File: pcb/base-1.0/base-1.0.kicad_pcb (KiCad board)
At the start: 2 copper layers, 85.6 x 54 mm, 178 parts, among them J101 USB_B_Micro, J102 UART, J103 74984104400, J104 Jack-DC, J105 USB_GPIO, J106 RPI_HEADER, Q101 BC817, Q102 BC817, Q103 DMP2305U-7, Q201 IRF7324TRPBF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

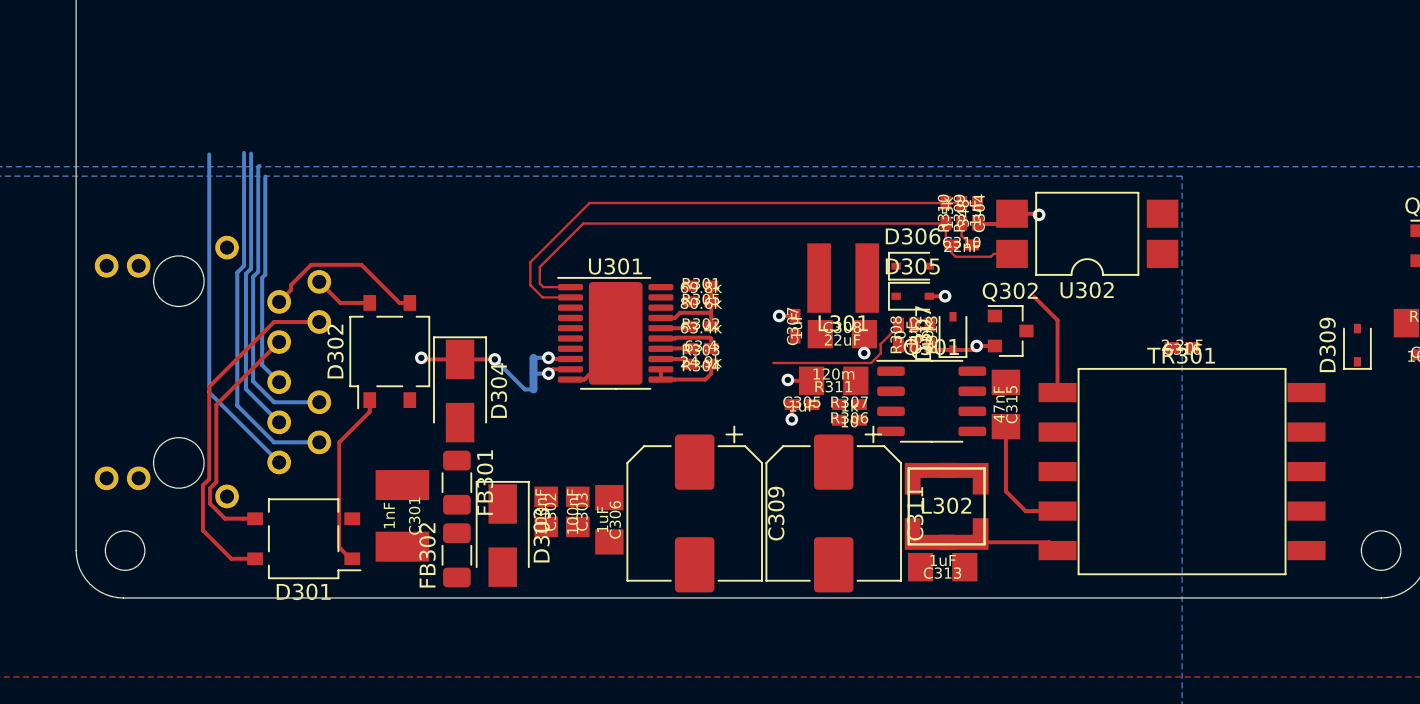
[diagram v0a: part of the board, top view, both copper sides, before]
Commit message: o Placing most of POE parts.
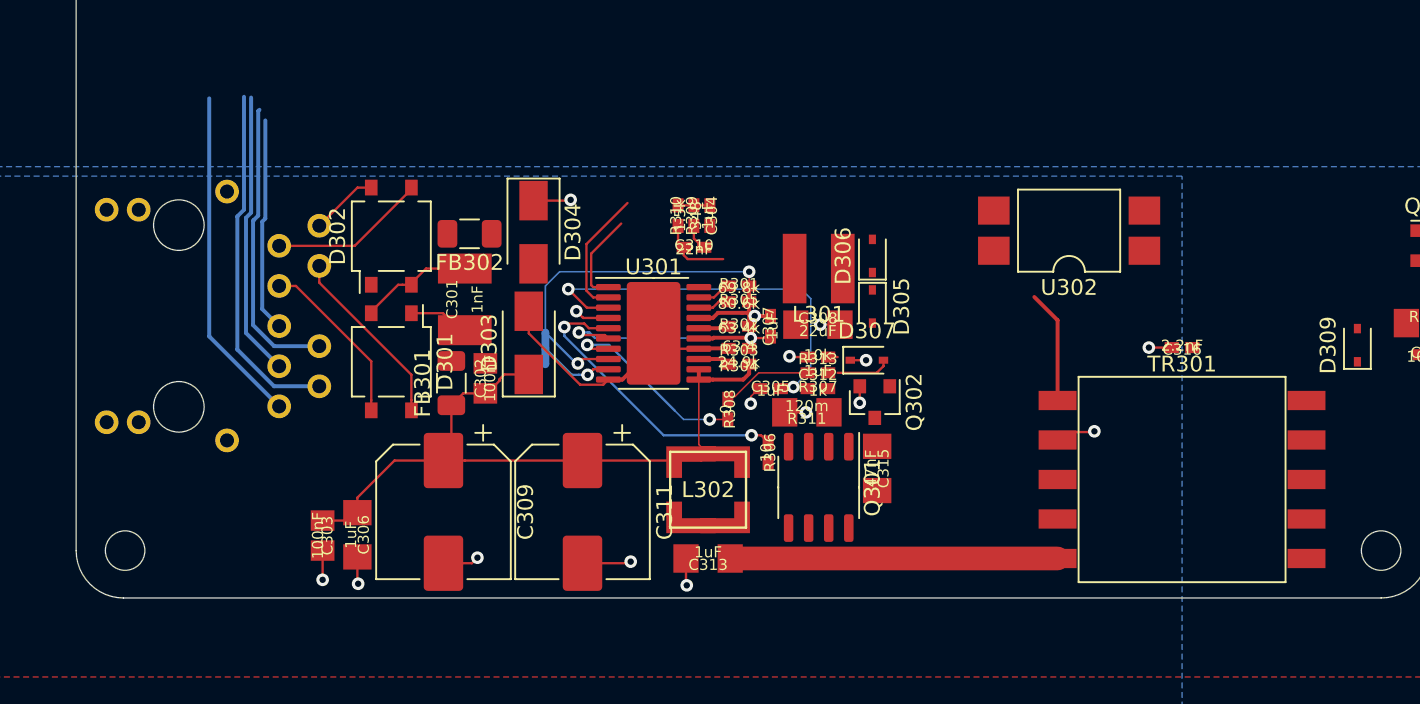
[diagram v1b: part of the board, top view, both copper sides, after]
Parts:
- moved FB302 20.4 mm to (132.9, 108.0), turned to 180 degrees
- moved R309 17.0 mm to (147.1, 106.8)
- moved R310 17.0 mm to (146.1, 106.8)
- moved C304 17.0 mm to (148.1, 106.8)
- moved C310 17.0 mm to (147.1, 108.8)
- moved C303 16.2 mm to (123.6, 127.0)
- moved C306 16.0 mm to (125.8, 127.0)
- moved C309 15.9 mm to (131.2, 125.5)
- moved C311 15.9 mm to (140.1, 125.5)
- moved L302 15.1 mm to (148.0, 124.2)
- moved C313 14.9 mm to (148.0, 128.5)
- moved C301 14.3 mm to (132.6, 112.1), turned to 90 degrees
- moved D301 12.5 mm to (128.0, 116.0), turned to 270 degrees
- moved D303 12.3 mm to (136.7, 114.8), turned to 90 degrees
- moved R308 11.8 mm to (149.2, 119.0), turned to 270 degrees
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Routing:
- net /PoE/ETH_VDD: track 4.59 -> 45.7 mm
- net /PoE/CS: track 0.00 -> 26.5 mm, vias 0 -> 2
- net /PoE/CTL: track 35.9 -> 10.4 mm
- net /PoE/VB: track 34.2 -> 10.2 mm
- net /PoE/ARTN: track 8.07 -> 27.7 mm, vias 1 -> 2
- net /PoE/GATE: track 0.00 -> 19.3 mm, vias 0 -> 2
- net /PoE/VC: track 0.00 -> 14.3 mm, vias 0 -> 2
- net Net-(C313-Pad1): track 7.24 -> 20.7 mm
- net /PoE/ETH_VSS: track 6.53 -> 17.7 mm
- net /PoE/Vin_A2: track 22.0 -> 11.6 mm
- net Net-(C315-Pad2): track 7.89 -> 0.00 mm
- net Net-(C301-Pad1): track 11.2 -> 3.95 mm
- net Net-(C301-Pad2): track 0.00 -> 7.21 mm
- net Net-(C312-Pad2): track 0.00 -> 5.32 mm
- net GND_ETH: track 22.1 -> 27.1 mm, vias 9 -> 16
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
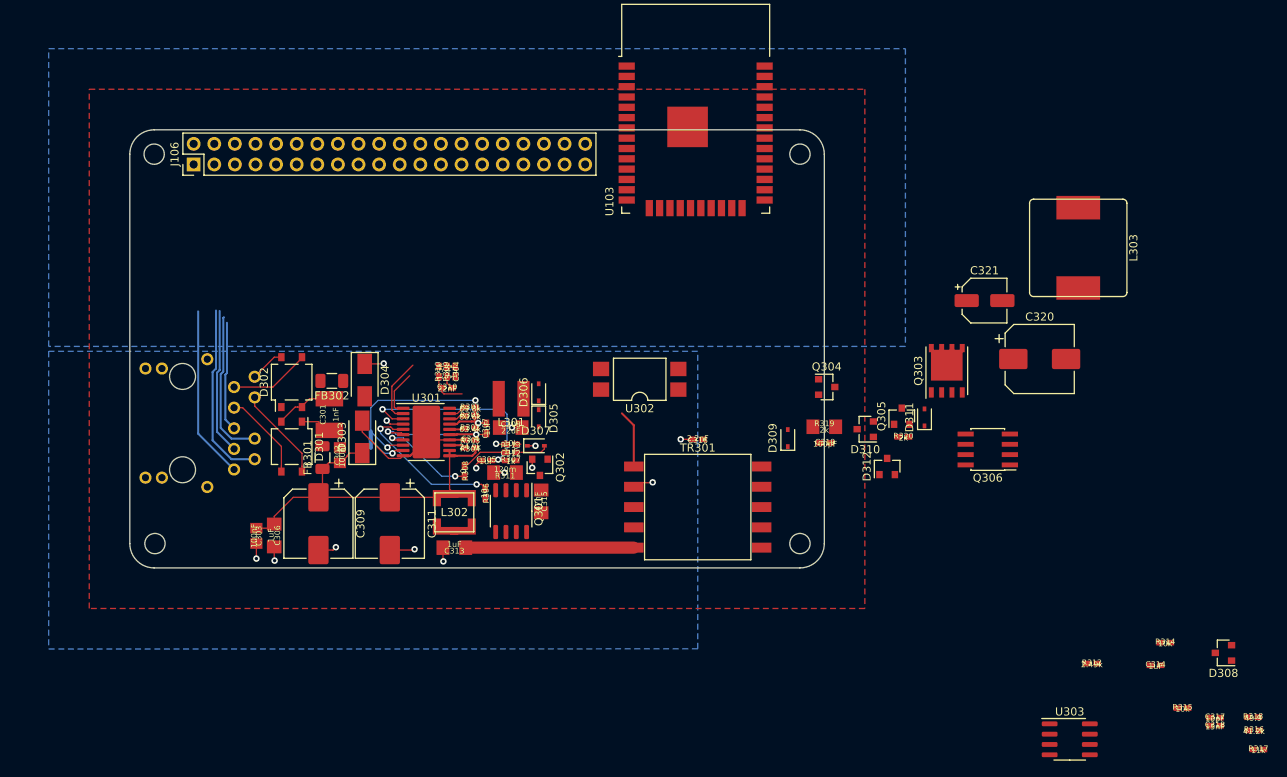
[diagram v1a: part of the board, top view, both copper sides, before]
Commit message: o Adjusting a couple of symbols. o PoE done for now.
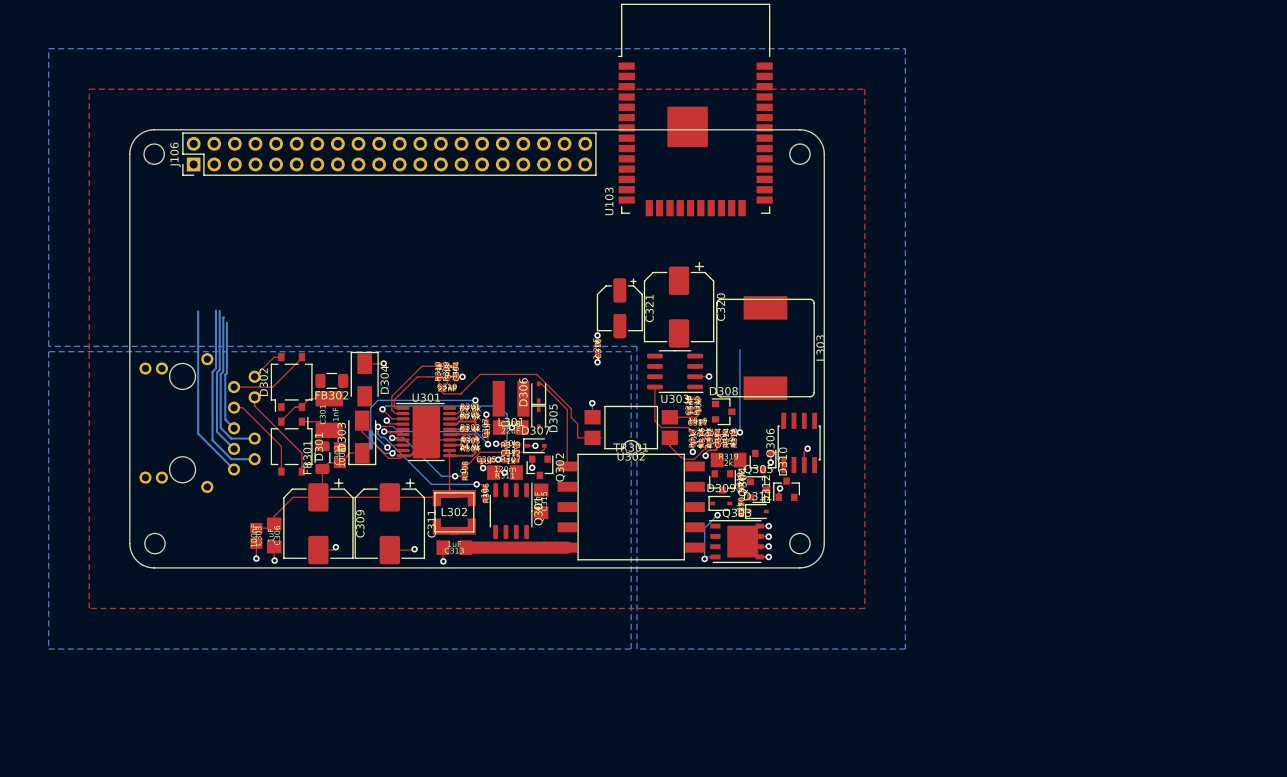
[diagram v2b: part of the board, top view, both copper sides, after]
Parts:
- moved R317 79.6 mm to (177.4, 115.0), turned to 90 degrees
- moved R316 77.1 mm to (178.4, 115.0), turned to 270 degrees
- moved C318 75.8 mm to (177.0, 111.0), turned to 90 degrees
- moved C317 73.4 mm to (178.0, 113.0), turned to 180 degrees
- moved R318 72.7 mm to (182.4, 115.0), turned to 270 degrees
- moved R315 70.4 mm to (178.0, 111.0), turned to 90 degrees
- moved D308 68.4 mm to (181.2, 111.8), turned to 0 degrees
- moved U303 66.5 mm to (175.2, 106.8), turned to 180 degrees
- moved C314 60.9 mm to (180.4, 115.0), turned to 270 degrees
- moved R314 59.8 mm to (181.4, 115.0), turned to 270 degrees
- moved R312 54.8 mm to (179.4, 115.0), turned to 270 degrees
- moved C321 45.0 mm to (168.4, 99.0), turned to 270 degrees
- moved C320 44.9 mm to (175.7, 98.8), turned to 270 degrees
- moved L303 40.5 mm to (186.3, 103.9)
- moved Q303 33.3 mm to (182.8, 127.8), turned to 0 degrees
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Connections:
- Q303 pad 1: GND -> /PoE/T_NEG
- Q303 pad 2: Net-(D309-Pad2) -> /PoE/T_NEG
- Q303 pad 4: (no net) -> Net-(D309-Pad2)
- Q303 pad 5: (no net) -> GND
- Q306 pad 1: /PoE/T_POS -> GND
- Q306 pad 2: Net-(D311-Pad2) -> GND
- Q306 pad 4: (no net) -> Net-(D311-Pad2)
- Q306 pad 5: (no net) -> /PoE/T_POS
- Q306 pad 6: (no net) -> /PoE/T_POS
- Q306 pad 7: (no net) -> /PoE/T_POS
- Q306 pad 8: (no net) -> /PoE/T_POS
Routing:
- net /PoE/CTL: track 10.4 -> 35.5 mm
- net GND: track 0.00 -> 17.7 mm, vias 0 -> 11
- net /Power mux/Vin_PoE: track 0.00 -> 11.0 mm, vias 0 -> 1
- net Net-(C317-Pad1): track 0.00 -> 9.52 mm
- net Net-(C313-Pad1): track 20.7 -> 12.5 mm
- net Net-(R312-Pad2): track 0.00 -> 7.51 mm
- net Net-(D309-Pad2): track 0.00 -> 7.49 mm, vias 0 -> 2
- net Net-(D306-Pad2): track 6.66 -> 11.8 mm
- net Net-(D308-Pad2): track 0.00 -> 4.78 mm
- net Net-(C317-Pad2): track 0.00 -> 4.71 mm
- net /PoE/VC: track 14.3 -> 17.3 mm
- net /PoE/VB: track 10.2 -> 12.6 mm
- net /PoE/GATE: track 19.3 -> 20.1 mm
- net GND_ETH: track 27.1 -> 26.8 mm, vias 16 -> 17
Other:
- net class Power added: clearance 0.2, trace_width 0.2, via_dia 0.8, via_drill 0.4

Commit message: o Much more PCB work.
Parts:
- RN101: value R_Network04 -> 49.9 Ω; footprint Resistor_THT:R_Array_SIP5 -> Resistor_SMD:R_Array_Convex_4x1206
- moved C102 204.1 mm to (227.8, 75.2)
- moved C101 163.8 mm to (226.3, 71.0)
- moved RN101 139.1 mm to (143.4, 103.7), turned to 180 degrees
- moved C114 136.3 mm to (162.7, 86.0)
- moved Q103 113.3 mm to (156.7, 104.0)
- moved U102 111.6 mm to (148.3, 103.9), turned to 90 degrees
- moved SW101 110.8 mm to (162.4, 89.9)
- moved C104 108.0 mm to (118.4, 125.3), turned to 180 degrees
- moved J102 103.3 mm to (126.7, 102.4), turned to 90 degrees
- moved U107 103.1 mm to (155.4, 86.7)
- moved Q203 102.2 mm to (161.5, 99.2)
- moved J101 101.9 mm to (109.5, 99.6), turned to 270 degrees
- moved R119 101.6 mm to (152.4, 102.9), turned to 180 degrees
- moved R118 99.9 mm to (152.4, 105.9), turned to 180 degrees
- moved R117 98.3 mm to (152.4, 104.9), turned to 180 degrees
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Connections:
- net Net-(NT201-Pad1) renamed /Power mux/Vin_PoE_sel
- net Net-(NT201-Pad2) renamed /Power mux/Vin_adapter_sel
- net Net-(NT201-Pad3) renamed /Power mux/Vin_USB_sel
- net Net-(U101-Pad3) renamed /D+
- net Net-(U101-Pad4) renamed /D-
- C107 pad 1: +3V3 -> +3V3_PHY
- C108 pad 1: +3V3 -> +3V3_PHY
- C120 pad 1: /BOOT -> /BOOT_3.3V
- C120 pad 2: /SW -> /SW_3.3V
- C121 pad 1: /BOOT -> /BOOT_12V
- C121 pad 2: /SW -> /SW_12V
- C122 pad 2: /FB -> /FB_3.3V
- C123 pad 2: /FB -> /FB_12V
- FB101 pad 2: +3V3 -> +3V3_PHY
- L101 pad 2: /SW -> /SW_3.3V
- L102 pad 2: /SW -> /SW_12V
- Q103 pad 1: +3V3 -> +3V3_PHY
- R103 pad 2: /FB -> /FB_3.3V
- R105 pad 1: /FB -> /FB_3.3V
- R109 pad 1: +3V3 -> +3V3_PHY
- R111 pad 2: /FB -> /FB_12V
- R116 pad 2: +3V3 -> +3V3_PHY
- R117 pad 1: +3V3 -> +3V3_PHY
- R118 pad 1: +3V3 -> +3V3_PHY
- R119 pad 1: +3V3 -> +3V3_PHY
- R120 pad 1: +3V3 -> +3V3_PHY
- R121 pad 1: /FB -> /FB_12V
- RN101 pad 1: +3V3 -> /ETH_RD+
- RN101 pad 3: /ETH_RD+ -> /ETH_TD+
- RN101 pad 5: /ETH_TD+ -> +3V3_PHY
- U102 pad 9: +3V3 -> +3V3_PHY
- U104 pad 1: Net-(J101-Pad2) -> Net-(J101-Pad3)
- U104 pad 6: Net-(J101-Pad3) -> Net-(J101-Pad2)
- U105 pad 2: /SW -> /SW_3.3V
- U105 pad 4: /FB -> /FB_3.3V
- U105 pad 6: /BOOT -> /BOOT_3.3V
- U106 pad 2: /SW -> /SW_12V
- U106 pad 4: /FB -> /FB_12V
- U106 pad 6: /BOOT -> /BOOT_12V
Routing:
- net /USB_TX: track 0.00 -> 21.7 mm, vias 0 -> 1
- net /Power mux/Vin_USB: track 0.00 -> 20.0 mm, vias 0 -> 2
- net +3V3: track 0.00 -> 19.6 mm, vias 0 -> 2
- net /USB_RX: track 0.00 -> 18.7 mm, vias 0 -> 1
- net Net-(C104-Pad1): track 18.0 -> 0.00 mm
- net /MCU_IO0: track 0.00 -> 13.1 mm
- net GND: track 17.7 -> 29.4 mm, vias 11 -> 17
- net /PoE/CTL: track 35.5 -> 24.8 mm
- net /RTS: track 0.00 -> 10.1 mm
- net /DTR: track 0.00 -> 9.93 mm
- net /MCU_RESET: track 0.00 -> 8.88 mm
- net /PoE/Vin_A1: track 10.9 -> 19.7 mm
- net /Power mux/Vin_adapter: track 0.00 -> 8.58 mm
- net Net-(R101-Pad2): track 0.00 -> 8.37 mm
- net /ETH_TD+: track 21.3 -> 13.8 mm
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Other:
- net class Default: via_dia 0.8 -> 0.5; via_drill 0.4 -> 0.25
- net class Power: via_drill 0.4 -> 0.3
- net class Power_0.8 added: clearance 0.3, trace_width 0.8, via_dia 0.8, via_drill 0.3
- rule via_min_drill: 0.3 -> 0.249
- rule via_min_size: 0.4 -> 0.25

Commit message: o More PCB work.
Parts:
- removed C109: 1uF, IPC-7351-CAPC:CAPC_1005x015
- removed NT301: Net-Tie_3_Tee, NetTie:NetTie-3_SMD_Pad0.5mm
- removed RN101: 49.9 Ω, Resistor_SMD:R_Array_Convex_4x1206
- added NT202: Net-Tie_2, NetTie:NetTie-2_SMD_Pad0.5mm, B.Cu at (152.2, 110.6)
- added NT203: Net-Tie_2, NetTie:NetTie-2_SMD_Pad0.5mm, F.Cu at (139.7, 116.5)
- added R124: 49.9, IPC-7351-RESC:RESC_1005x015, F.Cu at (143.8, 101.8)
- added R125: 49.9, IPC-7351-RESC:RESC_1005x015, F.Cu at (144.8, 101.8)
- added R126: 49.9, IPC-7351-RESC:RESC_1005x015, F.Cu at (141.8, 101.8)
- added R127: 49.9, IPC-7351-RESC:RESC_1005x015, F.Cu at (142.8, 101.8)
- TP101: moved to B.Cu
- moved C105 144.4 mm to (150.3, 108.4), turned to 270 degrees
- moved C111 133.8 mm to (146.2, 99.8), turned to 90 degrees
- moved FB101 112.6 mm to (145.9, 108.2), turned to 270 degrees
- moved C108 107.1 mm to (158.8, 103.8), turned to 90 degrees
- moved C112 104.6 mm to (148.3, 108.4), turned to 270 degrees
- moved C106 104.0 mm to (149.3, 108.4), turned to 270 degrees
- moved C107 103.1 mm to (152.4, 104.3)
- moved C110 102.3 mm to (147.3, 108.4), turned to 270 degrees
- moved TP101 98.7 mm to (151.8, 107.3)
- moved R108 97.1 mm to (144.4, 108.0), turned to 270 degrees
- moved R116 89.4 mm to (112.6, 122.1)
- moved R115 76.3 mm to (112.8, 104.7), turned to 180 degrees
- moved C113 72.1 mm to (109.8, 104.7)
- moved C114 34.0 mm to (174.6, 54.2)
- moved SW101 34.0 mm to (174.3, 58.1)
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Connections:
- net Net-(J101-Pad3) renamed /IN_D+
- C108 pad 1: +3V3_PHY -> +3V3
- D302 pad 4: /PoE/Vin_B2 -> /PoE/Vin_A1
- J101 pad 2: Net-(J101-Pad2) -> /IN_D-
- J103 pad 10: /PoE/Vin_B2 -> /PoE/Vin_A1
- J106 pad 11: /EXP_B1 -> /EXP_B6
- J106 pad 13: /EXP_B7 -> /EXP_B5
- J106 pad 15: /EXP_B2 -> /EXP_B4
- J106 pad 18: /EXP_B4 -> /EXP_B2
- J106 pad 21: /EXP_A7 -> /EXP_B1
- J106 pad 22: /EXP_B5 -> /EXP_B0
- J106 pad 24: /EXP_A6 -> /EXP_A7
- J106 pad 26: /EXP_A5 -> /EXP_A6
- J106 pad 27: /EXP_A0 -> /EXP_A5
- J106 pad 28: /EXP_A1 -> /EXP_A4
- J106 pad 31: /EXP_A4 -> /EXP_A2
- J106 pad 36: /EXP_B0 -> /EXP_A1
- J106 pad 37: /EXP_B6 -> /EXP_A0
- J106 pad 7: /EXP_A2 -> /EXP_B7
- R116 pad 2: +3V3_PHY -> /PHY_VDDA
- U102 pad 2: /ETH_GREEN_N -> /ETH_YELLOW_P
- U102 pad 3: /ETH_YELLOW_P -> /ETH_GREEN_N
- U104 pad 3: /D- -> /IN_D-
- U104 pad 4: /D+ -> /D-
- U104 pad 5: /Power mux/Vin_USB -> Net-(FB102-Pad2)
- U104 pad 6: Net-(J101-Pad2) -> /D+
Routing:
- net /ETH_YELLOW_P: track 0.00 -> 63.9 mm, vias 0 -> 1
- net /ETH_GREEN_N: track 0.00 -> 46.7 mm, vias 0 -> 1
- net GND: track 29.4 -> 47.7 mm, vias 17 -> 25
- net /EXP_B7: track 0.00 -> 14.9 mm
- net /MCU_IO0: track 13.1 -> 0.00 mm
- net /ETH_TD-: track 15.2 -> 2.36 mm, vias 0 -> 1
- net /PHY_VDDA: track 0.00 -> 12.4 mm, vias 0 -> 2
- net /IN_D-: track 0.00 -> 12.0 mm
- net /EXP_A6: track 0.00 -> 10.7 mm
- net /EXP_A5: track 0.00 -> 10.4 mm
- net /ETH_TD+: track 13.8 -> 3.88 mm, vias 0 -> 1
- net /IN_D+: track 2.46 -> 12.1 mm
- net /ETH_RD-: track 7.33 -> 16.8 mm, vias 0 -> 1
- net /PoE/CTL: track 24.8 -> 34.3 mm, vias 0 -> 2
- net /EXP_B0: track 0.00 -> 9.47 mm
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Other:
- net class Power_0.6 added: clearance 0.3, trace_width 0.6, via_dia 0.5, via_drill 0.25
- net class Power_0.8: clearance 0.3 -> 0.2
- net class Size_0.2__0.5 added: clearance 0.2, trace_width 0.2, via_dia 0.5, via_drill 0.25

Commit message: o More PCB work.
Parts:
- NT101, NT102, NT203: footprint NetTie:NetTie-2_SMD_Pad0.5mm -> UnlockOslo:NetTie-2_SMD_Pad0.15mm
- NT202: footprint NetTie:NetTie-2_SMD_Pad0.5mm -> UnlockOslo:NetTie-2_SMD_Pad0.20mm
- moved R112 58.0 mm to (179.8, 82.3)
- moved R113 58.0 mm to (182.8, 82.3)
- moved R114 58.0 mm to (177.8, 79.8)
- moved Q101 58.0 mm to (179.9, 80.1)
- moved Q102 58.0 mm to (183.3, 80.1)
- moved C203 23.8 mm to (127.8, 94.4), turned to 180 degrees
- moved R207 21.4 mm to (131.1, 97.8)
- moved R208 21.4 mm to (132.1, 97.8)
- moved R209 21.4 mm to (133.1, 97.8), turned to 270 degrees
- moved Q201 21.4 mm to (125.3, 91.2)
- moved R210 16.6 mm to (155.8, 87.8)
- moved R211 16.6 mm to (155.8, 86.8)
- moved R212 16.6 mm to (155.8, 85.8)
- moved U103 14.1 mm to (212.7, 92.1)
- moved NT102 12.5 mm to (121.8, 95.2)
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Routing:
- net /Power mux/Vin_USB: track 16.9 -> 72.1 mm, vias 6 -> 8
- net /ETH_TD+: track 3.88 -> 38.8 mm
- net /ETH_TD-: track 2.36 -> 35.9 mm
- net /MCU_RX: track 0.00 -> 28.5 mm
- net /MCU_TX: track 0.00 -> 24.0 mm
- net /ETH_RD-: track 16.8 -> 35.9 mm
- net /ETH_RD+: track 18.0 -> 33.7 mm
- net /USB_TX: track 15.7 -> 0.00 mm, vias 1 -> 0
- net /USB_RX: track 15.0 -> 0.00 mm, vias 1 -> 0
- net Net-(C204-Pad1): track 0.00 -> 13.8 mm, vias 0 -> 1
- net Net-(Q201-Pad2): track 0.00 -> 11.2 mm
- net GND: track 47.7 -> 57.5 mm, vias 25 -> 29
- net Net-(C205-Pad1): track 0.00 -> 7.61 mm
- net /ETH_YELLOW_P: track 63.9 -> 56.6 mm
- net Net-(D103-Pad1): track 0.00 -> 6.15 mm
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
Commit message: o More PCB work.
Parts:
- removed NT201: Net-Tie_3_to_1, NetTie:NetTie-4_SMD_Pad0.5mm
- added NT301: Net-Tie_3, UnlockOslo:NetTie-3_SMD_Pad0.5mm_132, B.Cu at (125.5, 92.0)
- added NT302: Net-Tie_3, UnlockOslo:NetTie-3_SMD_Pad0.5mm_132, B.Cu at (141.8, 95.9)
- moved R210 26.1 mm to (131.9, 98.3), turned to 90 degrees
- moved R211 25.6 mm to (132.9, 98.3), turned to 90 degrees
- moved R212 25.2 mm to (133.9, 98.3), turned to 90 degrees
- moved Q203 23.1 mm to (138.6, 96.6), turned to 90 degrees
- moved C206 21.7 mm to (135.3, 99.1)
- moved R208 7.04 mm to (129.8, 91.1)
- moved R207 5.29 mm to (127.0, 94.4), turned to 0 degrees
- moved R209 4.92 mm to (129.8, 94.1), turned to 90 degrees
- moved C203 3.80 mm to (124.0, 94.4)
- moved C128 2.64 mm to (132.3, 85.8)
- moved U201 1.05 mm to (133.2, 93.0), turned to 0 degrees
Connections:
- net Net-(R201-Pad2) renamed /Power mux/UV3
- net Net-(R202-Pad2) renamed /Power mux/OV3
- net Net-(R204-Pad2) renamed /Power mux/UV2
- net Net-(R205-Pad2) renamed /Power mux/OV2
- net Net-(R207-Pad2) renamed /Power mux/UV1
- net Net-(R208-Pad2) renamed /Power mux/OV1
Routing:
- net GND: track 57.5 -> 96.2 mm, vias 29 -> 31
- net /EXP_A0: track 0.00 -> 23.7 mm
- net /EXP_A1: track 0.00 -> 22.3 mm
- net Net-(Q202-Pad2): track 5.41 -> 26.7 mm, vias 0 -> 2
- net Net-(NT301-Pad2): track 0.00 -> 18.6 mm
- net /EXP_A2: track 0.00 -> 15.5 mm
- net /DTR: track 2.88 -> 18.2 mm, vias 0 -> 1
- net /EXP_A4: track 0.00 -> 14.3 mm
- net Net-(C205-Pad1): track 7.61 -> 21.0 mm, vias 0 -> 2
- net /Power mux/Vin_adapter: track 16.4 -> 29.2 mm, vias 0 -> 2
- net /EXP_A3: track 0.00 -> 12.7 mm
- net /Power mux/UV1: track 1.00 -> 13.4 mm
- net /Power mux/OV2: track 0.00 -> 11.2 mm, vias 0 -> 2
- net Net-(Q201-Pad2): track 11.2 -> 21.5 mm, vias 0 -> 2
- net /Power mux/Vin_adapter_sel: track 0.00 -> 9.82 mm, vias 0 -> 1
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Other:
- net class Size_0.10__0.5 added: clearance 0.1, trace_width 0.1, via_dia 0.5, via_drill 0.25
